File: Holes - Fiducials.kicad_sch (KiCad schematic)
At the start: 10 parts

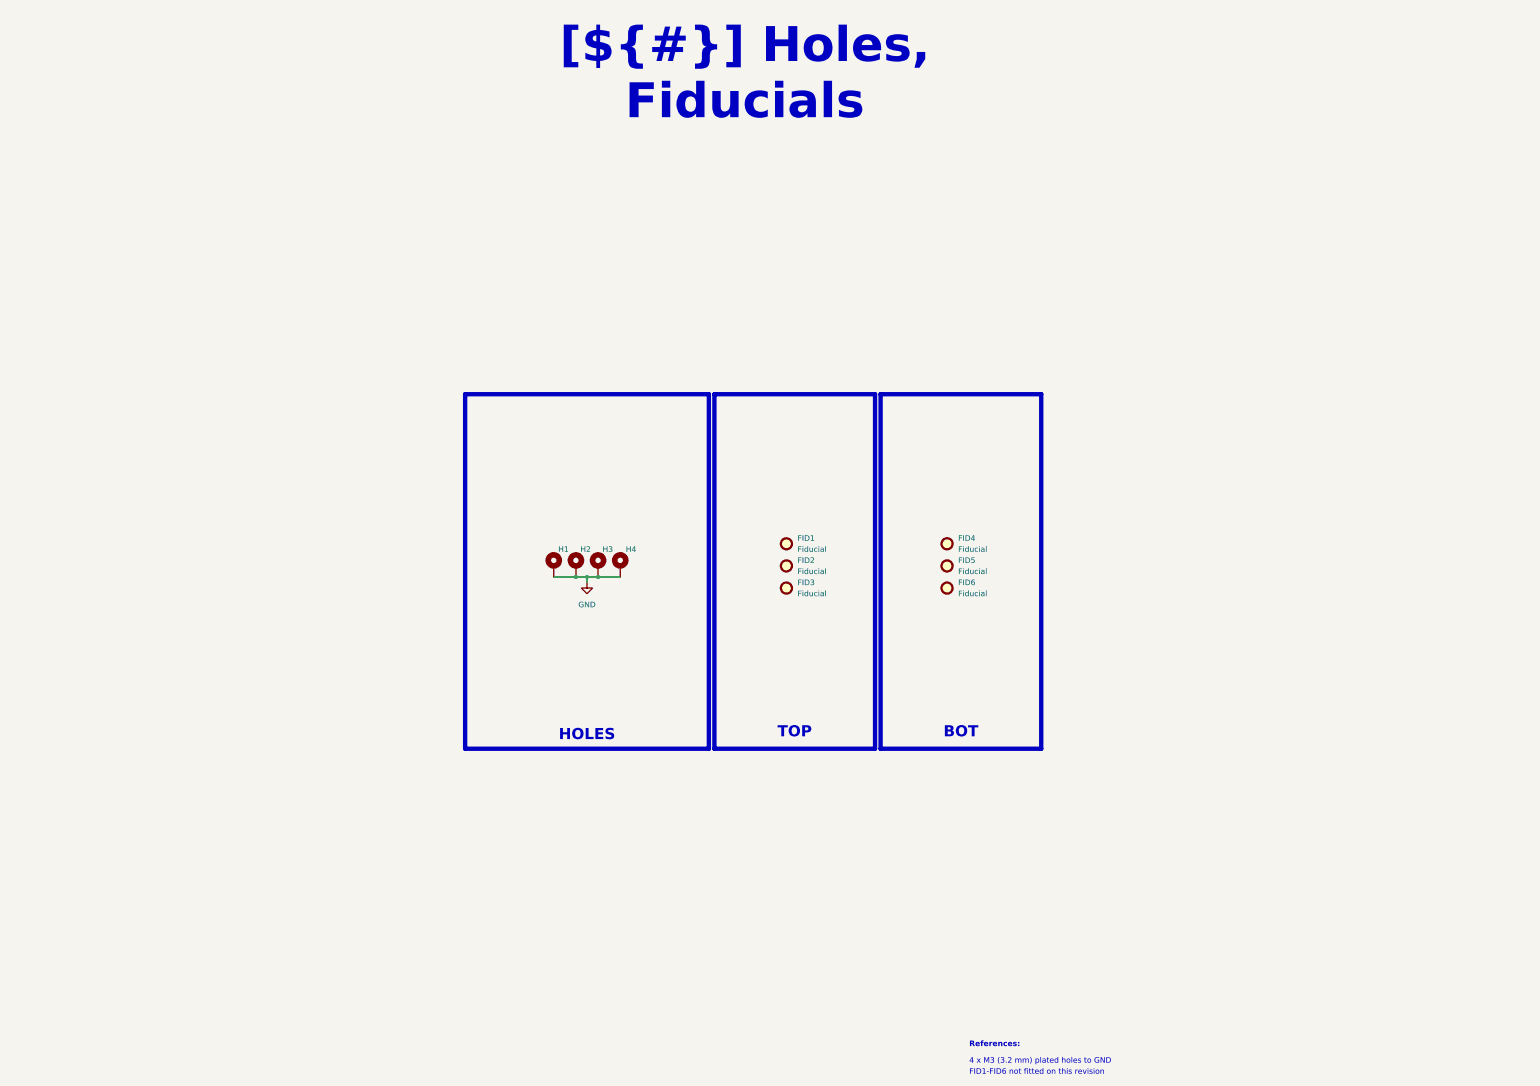
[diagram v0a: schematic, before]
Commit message: Restyle the schematic like OPEN_PHASE, merge the power sheets, rework the bottom silkscreen
- Schematic: all sheets on A3 in the OPEN_PHASE look (red header bands,
  DESCRIPTION / DESIGN NOTE / LAYOUT NOTE / CALCULS & BUDGET panels in
  French, TEST POINTS panel, References in the title block)
- Title block: INGENIERIE FRANCE logo in KDT_Template_GIT.kicad_wks,
  per-sheet logo images removed
- Power - Sequencing rebuilt with curves from LTspice simulations 01-04
- TPS61086 and LT3042 sheets merged into Power Supply - Analog Rails
  (page 5, keeps the TPS sheet UUID); pages renumbered to 9, local nets
  renamed to /Project Architecture/Power_Supply/*, PCB links updated
- PCB: per-rail net colours (+3.3V, +6V, +5VA, GND) as on OPEN_PHASE
- PCB B.SilkS: test point pills with Arial Black knockout names, J1
  pinout cells, E+/E-/S+/S- tags on the M12 pads, CELL 1 / CELL 2 titles
  and a LOAD CELL wiring panel

Netlist connectivity, ERC (2 warnings) and copper DRC unchanged;
schematic parity clean.

Co-Authored-By: Claude Opus 5.5 <noreply@anthropic.com>
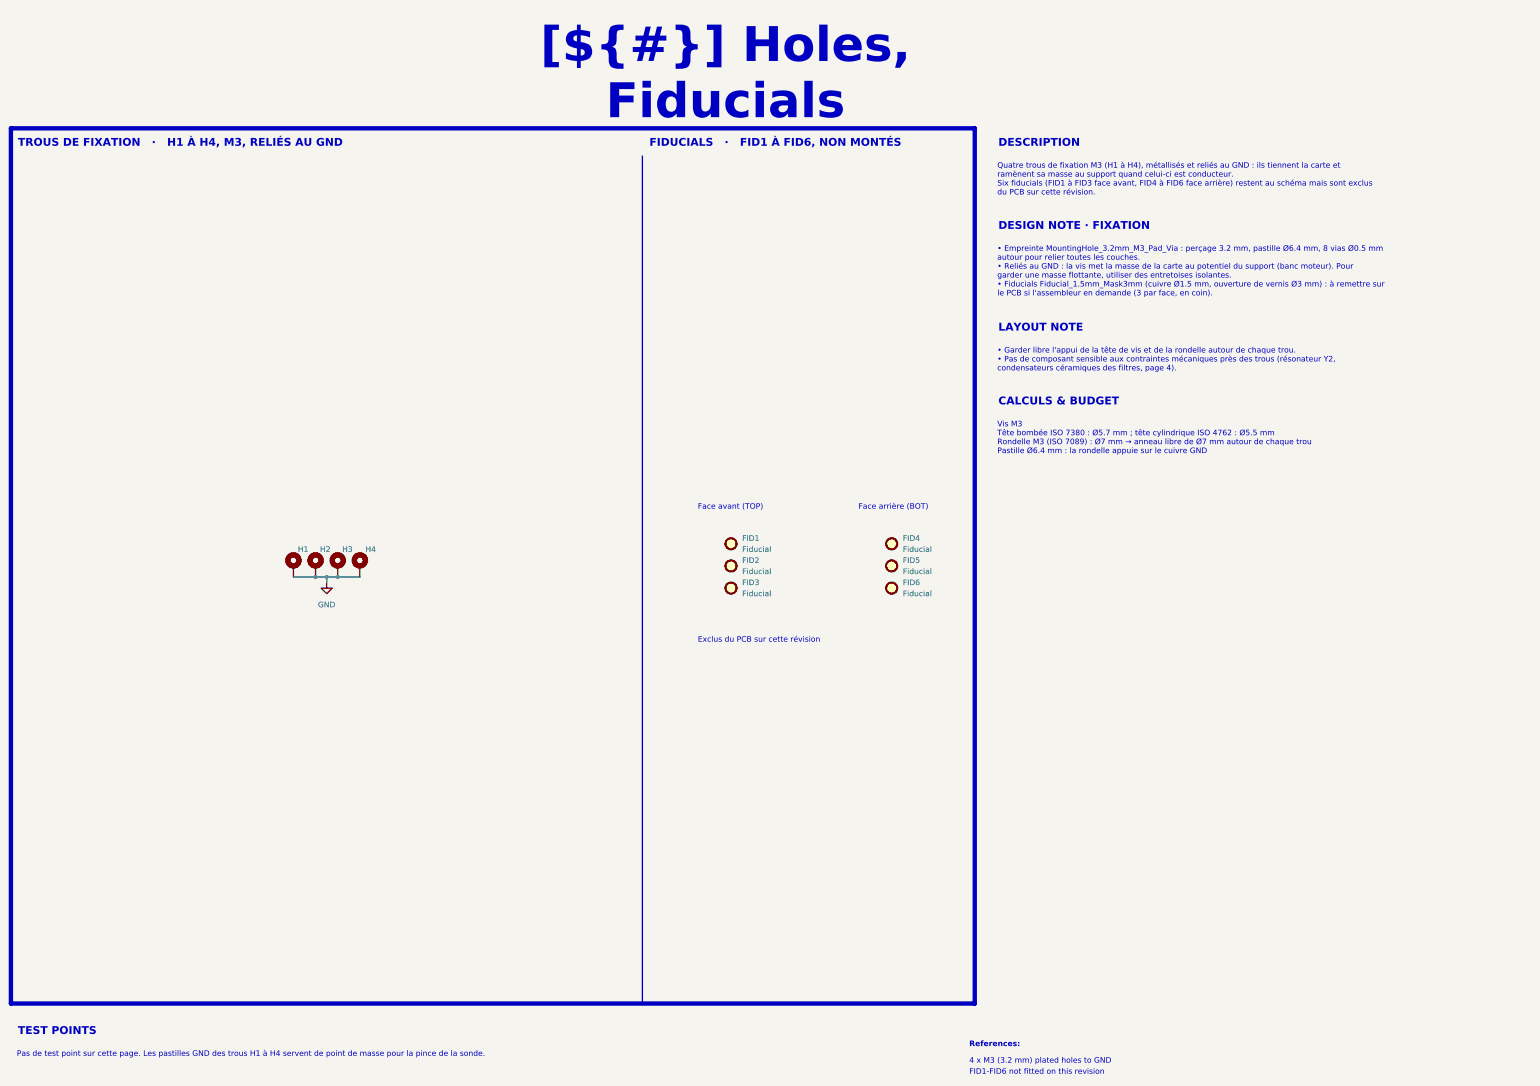
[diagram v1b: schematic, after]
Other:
- note added: "Exclus du PCB sur cette révision"
- note added: "Face arrière (BOT)"
- note added: "Face avant (TOP)"
- moved on the sheet: FID1, FID2, FID3, FID4, FID5, FID6, H1, H2, H3, H4
